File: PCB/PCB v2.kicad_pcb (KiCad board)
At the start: 4 copper layers, 56 x 45 mm, 132 parts, among them J2 USB_C_Receptacle_PowerOnly_6P, J3 6871XX182122_687110182122, J5 Conn_01x03_Pin, J7 Conn_02x06_Odd_Even, U1 TPD2E2U06DCK, U11 OPA4350EA_250, U12 OPA4350EA_250, U13 OPA4350EA_250, U2 ADS131M08xPBS, U3 74LVC1G17, U4 LM27762, U6 OPA4350EA_250, U7 LP5907MFX-3.3

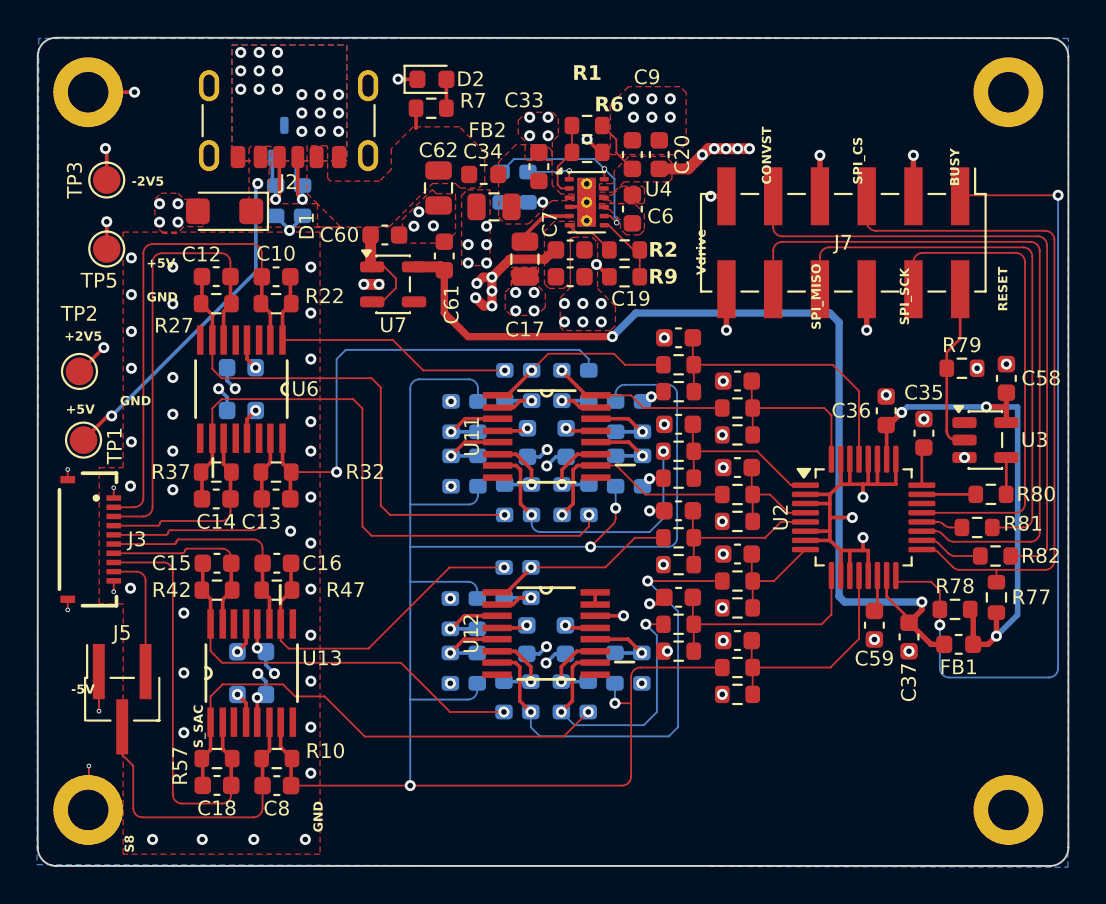
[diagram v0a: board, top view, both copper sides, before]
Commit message: Silkscreen: label the dense blocks, add channel labels and J7 pin names
Dense blocks: 0.5 mm references
- All 56 references in the dense blocks are now shown at 0.5 x 0.5 mm,
  stroke 0.12 mm.
- Divider block (front): each label sits on its part's own row. The
  left column (AIN0/2/4/6 triples) is labeled down its left side, the
  right column (AIN1/3/5/7) down its right side, so the labels read as
  two aligned lists.
  - Where a GND via sits right beside a pad, the label is allowed over
    the via's ring (vias are tented both sides) but never over the
    drill. R74 is labelled below its part.
- Diff-amp resistors and C23-C26 (back): each label is next to its own
  part and closer to it than to any neighbour.

Per-channel labels, 0.8 mm
- CH1-CH7 on B.SilkS, next to each diff-amp's four-resistor group.
  Each label is kept well clear of other channels' parts, so it can't
  be read as the wrong channel.
- AIN0-AIN7 on B.SilkS, directly behind each divider C / Rs / Rsh
  triple. There is no room for 0.8 mm text on the front between the
  two 3.2 mm-pitch columns; the back is empty there.
- Channel map (from the schematic note): AIN0=Vout1, AIN1=Vout4,
  AIN2=Vout2, AIN3=Vout3, AIN4=Vout5, AIN5=Vout6, AIN6=Vout7,
  AIN7=Vsac.

J7 pin names, 0.8 mm
- Removed the seven old 0.5 mm texts (Vdrive, CONVST, SPI_MISO,
  SPI_CS, SPI_SCK, BUSY, RESET). They were AD7606-era names and sat
  on the pads.
- New labels, outboard of each pad:
  - odd row (above): SYNC, GND, CS, GND, DRDY, GND (pins 1-11);
  - even row (below): CLK, MOSI, GND, MISO, SCLK, GND (pins 2-12).
- The odd-row labels are bottom-aligned at a common gap. CLK and the
  pin-12 GND are horizontal because R79 or a via sits right below
  those pads.
- To make room, the C35, C36, C58, R79 and U2 references were
  re-placed with the same rules as before.

Only silkscreen changes: no footprint, track, via or zone moved.
DRC: no new silk_overlap or silk_over_copper items; the text_height
warnings rise from 17 to 66, a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
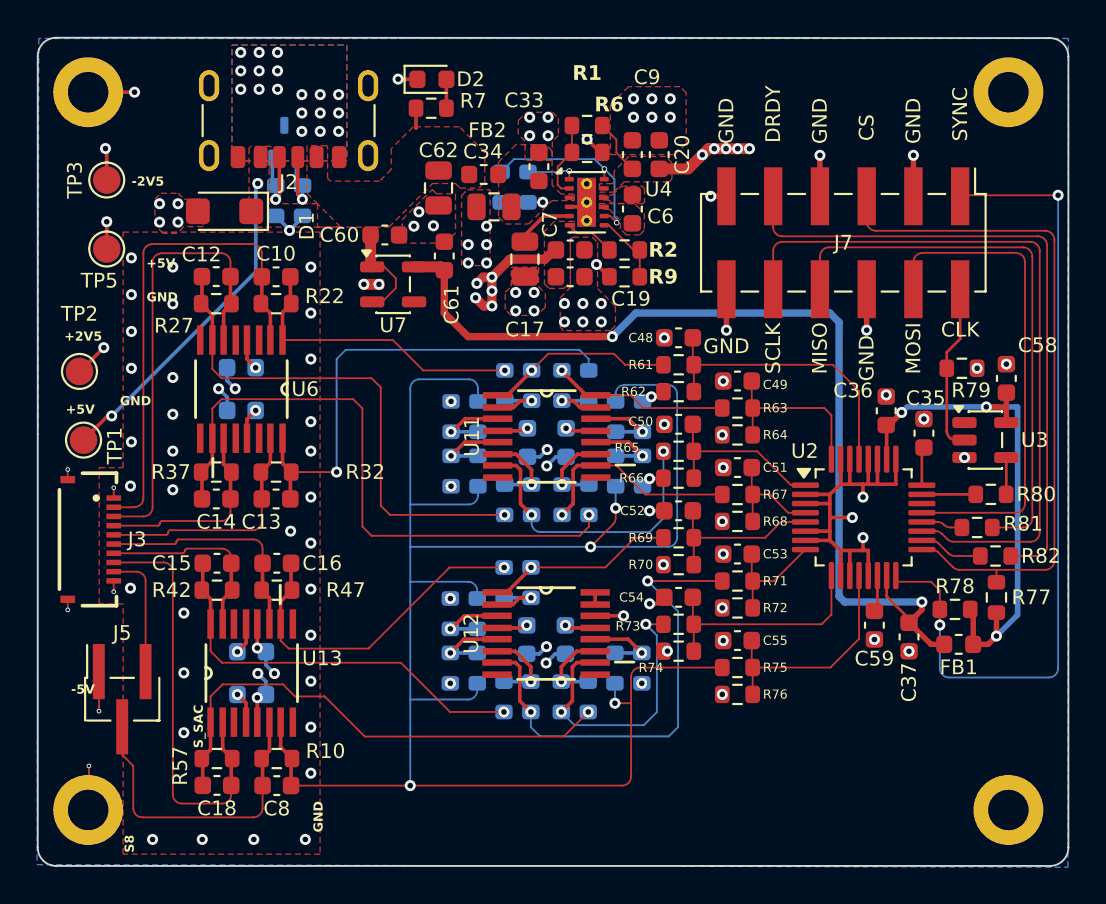
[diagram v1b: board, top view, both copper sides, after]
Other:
- board text added: "AIN0"
- board text added: "AIN1"
- board text added: "AIN2"
- board text added: "AIN3"
- board text added: "AIN4"
- board text added: "AIN5"
- board text added: "AIN6"
- board text added: "AIN7"
- board text added: "CH1"
- board text added: "CH2"
- board text added: "CH3"
- board text added: "CH4"
- board text added: "CH5"
- board text added: "CH6"
- board text added: "CH7"
- board text added: "CLK"
- board text added: "CS"
- board text added: "DRDY"
- board text added: "MISO"
- board text added: "MOSI"
- board text added: "SCLK"
- board text added: "SYNC"
- board text removed: "BUSY"
- board text removed: "CONVST"
- board text removed: "RESET"
- board text removed: "SPI_CS"
- board text removed: "SPI_MISO"
- board text removed: "SPI_SCK"
- board text removed: "Vdrive"

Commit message: Silkscreen: fix stale power and J5 labels
Several 0.5 mm user texts dated from an earlier layout and no longer
matched the parts next to them.

- TP5 (GND): the "+5V" text beside it becomes "GND", placed the way
  TP3's "-2V5" label is. The duplicate loose "GND" just below it,
  at (127.17, 90.43), is removed.
- Removed an orphan "-5V" at (123.07, 111.74). No -5V net exists on
  this board, and the text also sat on J5 pin 1 (silk_over_copper).
- Removed a loose "GND" at (125.72, 96.07), between TP2 and TP1. It
  labelled no test point.
- J5: the old "S8", "S_SAC" and "GND" texts were left at the previous
  2.54 mm J5 position. They are replaced by pin labels at the 1.27 mm
  J5: GND above pin 1, S8 above pin 3 (either side of the J5
  designator), S_SAC to the left of pin 2.

Every remaining user text now labels an adjacent pin or test point:
- +2V5 at TP2, +5V at TP1, -2V5 at TP3, GND at TP5;
- GND, S_SAC and S8 at J5.
New labels keep the existing style: 0.5 mm, bold, knockout.

DRC: silk_over_copper 1 -> 0, silk_overlap 3 -> 2, text_height
66 -> 63. No footprint, track, via or zone moved.

Co-Authored-By: Claude Opus 5.5 <noreply@anthropic.com>
Claude-Session: https://claude.ai/code/session_01TYMP7BCHvS3DvLnCv8UeQA
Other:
- board text removed: "-5V"
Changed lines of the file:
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@@
-		)
-	)
-	(gr_text "-5V"
-		(at 123.07 111.74 0)
-		(layer "F.SilkS" knockout)
-		(effects
-			(font
-				(size 0.5 0.5)
-				(thickness 0.125)
-				(bold yes)
-			)
-			(justify left bottom)
-		)
-	)
-	(gr_text "GND\n"
-		(at 125.72 96.07 0)
-		(layer "F.SilkS" knockout)
-		(effects
-			(font
-				(size 0.5 0.5)
-				(thickness 0.125)
-				(bold yes)
-			)
-			(justify left bottom)
 		)
 	)
@@
 		)
 	)
-	(gr_text "+5V"
-		(at 127.16 88.59 0)
-		(layer "F.SilkS" knockout)
-		(effects
-			(font
-				(size 0.5 0.5)
-				(thickness 0.125)
-				(bold yes)
-			)
-			(justify left bottom)
-		)
-	)
-	(gr_text "GND\n"
-		(at 127.17 90.43 0)
-		(layer "F.SilkS" knockout)
-		(effects
-			(font
-				(size 0.5 0.5)
-				(thickness 0.125)
-				(bold yes)
-			)
-			(justify left bottom)
-		)
-	)
-	(gr_text "S8"
-		(at 126.54 120.32 90)
-		(layer "F.SilkS" knockout)
-		(effects
-			(font
-				(size 0.5 0.5)
-				(thickness 0.125)
-				(bold yes)
-			)
-			(justify left bottom)
-		)
-	)
-	(gr_text "S_SAC"
-		(at 130.29 114.64 90)
+	(gr_text "GND"
+		(at 126.36 87.89 0)
 		(layer "F.SilkS" knockout)
 		(effects
@@
 	)
 	(gr_text "GND"
-		(at 136.8 119.22 90)
+		(at 123.38 108.48 0)
 		(layer "F.SilkS" knockout)
 		(effects
@@
 				(bold yes)
 			)
-			(justify left bottom)
 		)
 	)
+	(gr_text "S_SAC"
+		(at 124.1 113.73 0)
+		(layer "F.SilkS" knockout)
+		(effects
+			(font
+				(size 0.5 0.5)
+				(thickness 0.125)
+				(bold yes)
+			)
+		)
+	)
+	(gr_text "S8"
+		(at 128.12 108.48 0)
+		(layer "F.SilkS" knockout)
+		(effects
+			(font
+				(size 0.5 0.5)
+				(thickness 0.125)
+				(bold yes)
+			)
+		)
+	)

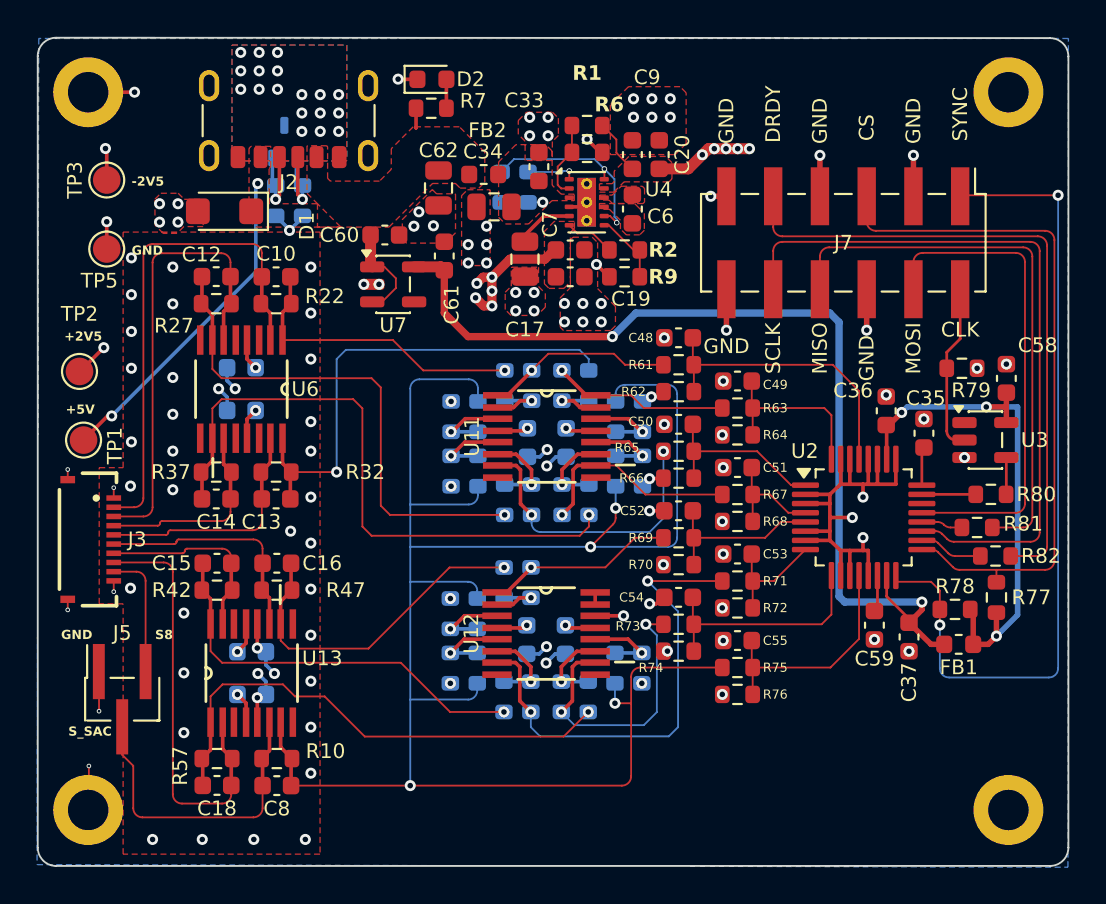
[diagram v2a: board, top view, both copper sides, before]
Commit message: Fix op-amp pin-1 marking, re-place four labels, reroute TP3's -2V5 via
Designer edits made in pcbnew after the pre-order review.

- Opa4 footprint (U6, U11, U12, U13): the silkscreen pin-1 marker now
  sits at pin 1.
  - The notch was on the body edge, so the placed IC hid it.
  - The only visible mark was a bar beside the pin 9/10 corner, which
    read as pin 1 at the wrong end. Fitting the part 180 deg round
    would put the supplies on the inputs.
  - The embedded footprint's unit table is dropped as well.
  - This also clears both DRC silk_overlap items (R37/U6, U13/R47).
- Re-placed the C9, C19, R1 and R6 reference labels. The review found
  them sitting on, or equidistant from, a neighbouring part.
- TP3 (-2V5): the via moves from (124.94, 82.06) to (127.21, 83.05),
  fed by a 0.2 mm F.Cu stub from the test point.

Co-Authored-By: Claude Opus 5.5 <noreply@anthropic.com>
Claude-Session: https://claude.ai/code/session_01TYMP7BCHvS3DvLnCv8UeQA
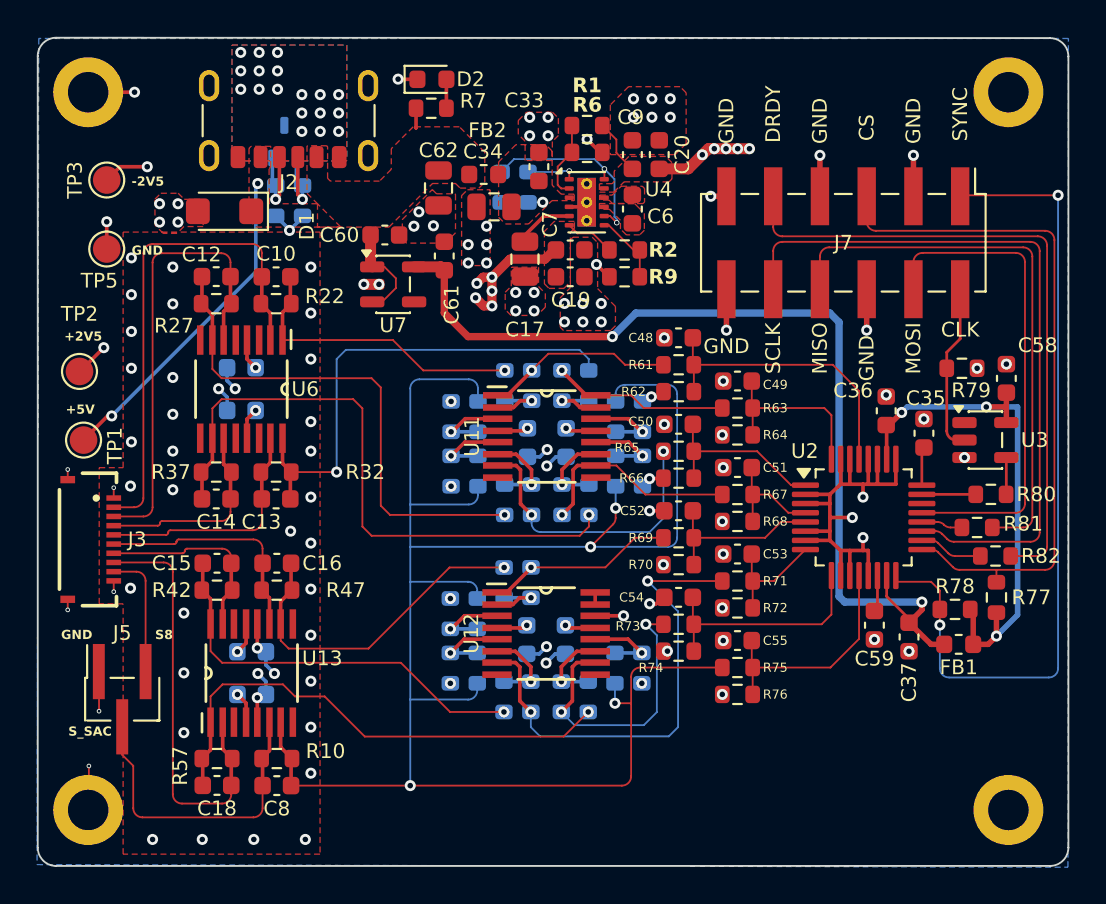
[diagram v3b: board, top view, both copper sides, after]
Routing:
- net -2V5: track 18.9 -> 19.7 mm
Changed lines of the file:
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@@
 		(tags "capacitor")
 		(property "Reference" "C19"
-			(at -3.3 -1.2 0)
+			(at -0.03 -1.25 180)
 			(layer "F.SilkS")
 			(effects
@@
 		(tags "capacitor")
 		(property "Reference" "C9"
-			(at 4.2 0.8 0)
+			(at 2.03 -0.09 0)
 			(layer "F.SilkS")
 			(effects
@@
 		(sheetname "/SENSORS/")
 		(sheetfile "FOGLIO2.kicad_sch")
-		(units
-			(unit
-				(name "A")
-				(pins "3" "2" "8" "9" "1")
-			)
-			(unit
-				(name "B")
-				(pins "5" "6" "7")
-			)
-			(unit
-				(name "C")
-				(pins "12" "11" "10")
-			)
-			(unit
-				(name "D")
-				(pins "14" "15" "16")
-			)
-			(unit
-				(name "E")
-				(pins "4" "13")
-			)
-		)
 		(attr smd)
 		(duplicate_pad_numbers_are_jumpers no)
@@
 		)
 		(fp_line
-			(start 4.7752 1.5494)
-			(end 3.7592 1.5494)
+			(start -0.3048 -2.4892)
+			(end -1.5494 -2.4892)
 			(stroke
 				(width 0.1524)
@@
 		)
 		(fp_line
-			(start -0.3048 -2.4892)
-			(end -1.5494 -2.4892)
+			(start 0.3048 -2.4892)
+			(end -0.3048 -2.4892)
 			(stroke
 				(width 0.1524)
@@
 		)
 		(fp_line
-			(start 0.3048 -2.4892)
-			(end -0.3048 -2.4892)
+			(start 1.5494 -2.4892)
+			(end 0.3048 -2.4892)
 			(stroke
 				(width 0.1524)
@@
 		)
 		(fp_line
-			(start 1.5494 -2.4892)
-			(end 0.3048 -2.4892)
+			(start -2.192 -2.7)
+			(end -3.208 -2.7)
 			(stroke
 				(width 0.1524)
@@
 		(tags "SparkFun resistor")
 		(property "Reference" "R6"
-			(at 1.2 -2.6 0)
+			(at 0.01 -2.58 0)
 			(layer "F.SilkS")
 			(effects
@@
 		(sheetname "/SENSORS/")
 		(sheetfile "FOGLIO2.kicad_sch")
-		(units
-			(unit
-				(name "A")
-				(pins "3" "2" "8" "9" "1")
-			)
-			(unit
-				(name "B")
-				(pins "5" "6" "7")
-			)
-			(unit
-				(name "C")
-				(pins "12" "11" "10")
-			)
-			(unit
-				(name "D")
-				(pins "14" "15" "16")
-			)
-			(unit
-				(name "E")
-				(pins "4" "13")
-			)
-		)
 		(attr smd)
 		(duplicate_pad_numbers_are_jumpers no)
 		(fp_line
+			(start -2.192 -2.7)
+			(end -3.208 -2.7)
+			(stroke
+				(width 0.1524)
+				(type solid)
+			)
+			(layer "F.SilkS")
+		)
+		(fp_line
 			(start -1.5494 2.4892)
 			(end 1.5494 2.4892)
@@
 			(layer "F.SilkS")
 		)
-		(fp_line
-			(start 4.7752 1.5494)
-			(end 3.7592 1.5494)
-			(stroke
-				(width 0.1524)
-				(type solid)
-			)
-			(layer "F.SilkS")
-		)
 		(fp_arc
 			(start 0.3048 -2.4892)
@@
 		(tags "SparkFun resistor")
 		(property "Reference" "R1"
-			(at 0 2.85 0)
+			(at 0 2.18 0)
 			(layer "F.SilkS")
 			(effects
@@
 		(sheetname "/SENSORS/")
 		(sheetfile "FOGLIO2.kicad_sch")
-		(units
-			(unit
-				(name "A")
-				(pins "3" "2" "8" "9" "1")
-			)
-			(unit
-				(name "B")
-				(pins "5" "6" "7")
-			)
-			(unit
-				(name "C")
-				(pins "12" "11" "10")
-			)
-			(unit
-				(name "D")
-				(pins "14" "15" "16")
-			)
-			(unit
-				(name "E")
-				(pins "4" "13")
-			)
-		)
 		(attr smd)
 		(duplicate_pad_numbers_are_jumpers no)
 		(fp_line
-			(start 1.5494 -2.4892)
-			(end 0.3048 -2.4892)
+			(start -2.192 -2.7)
+			(end -3.208 -2.7)
 			(stroke
 				(width 0.1524)
@@
 		)
 		(fp_line
-			(start 0.3048 -2.4892)
-			(end -0.3048 -2.4892)
+			(start 1.5494 -2.4892)
+			(end 0.3048 -2.4892)
 			(stroke
 				(width 0.1524)
@@
 		)
 		(fp_line
-			(start -0.3048 -2.4892)
-			(end -1.5494 -2.4892)
+			(start 0.3048 -2.4892)
+			(end -0.3048 -2.4892)
 			(stroke
 				(width 0.1524)
@@
 		)
 		(fp_line
-			(start 4.7752 1.5494)
-			(end 3.7592 1.5494)
+			(start -0.3048 -2.4892)
+			(end -1.5494 -2.4892)
 			(stroke
 				(width 0.1524)
@@
 		(sheetname "/SENSORS/")
 		(sheetfile "FOGLIO2.kicad_sch")
-		(units
-			(unit
-				(name "A")
-				(pins "3" "2" "8" "9" "1")
-			)
-			(unit
-				(name "B")
-				(pins "5" "6" "7")
-			)
-			(unit
-				(name "C")
-				(pins "12" "11" "10")
-			)
-			(unit
-				(name "D")
-				(pins "14" "15" "16")
-			)
-			(unit
-				(name "E")
-				(pins "4" "13")
-			)
-		)
 		(attr smd)
 		(duplicate_pad_numbers_are_jumpers no)
 		(fp_line
+			(start -2.184 -2.7)
+			(end -3.2 -2.7)
+			(stroke
+				(width 0.1524)
+				(type solid)
+			)
+			(layer "F.SilkS")
+		)
+		(fp_line
 			(start -1.5494 2.4892)
 			(end 1.5494 2.4892)
@@
 			(layer "F.SilkS")
 		)
-		(fp_line
-			(start 4.7752 1.5494)
-			(end 3.7592 1.5494)
-			(stroke
-				(width 0.1524)
-				(type solid)
-			)
-			(layer "F.SilkS")
-		)
 		(fp_arc
 			(start 0.3048 -2.4892)
@@
 	)
 	(segment
-		(start 125.009426 83.771476)
-		(end 125.009426 82.129426)
-		(width 0.2)
-		(layer "F.Cu")
-		(net "-2V5")
-	)
-	(segment
-		(start 125.009426 82.129426)
-		(end 124.94 82.06)
-		(width 0.2)
-		(layer "F.Cu")
-		(net "-2V5")
-	)
-	(segment
 		(start 132.5804 107.895)
 		(end 132.5804 108.9314)
@@
 	)
 	(segment
+		(start 127.21 83.05)
+		(end 125.730902 83.05)
+		(width 0.2)
+		(layer "F.Cu")
+		(net "-2V5")
+	)
+	(segment
 		(start 150.071529 108.109044)
 		(end 149.931329 107.968844)
@@
 	)
 	(segment
+		(start 125.730902 83.05)
+		(end 125.009426 83.771476)
+		(width 0.2)
+		(layer "F.Cu")
+		(net "-2V5")
+	)
+	(segment
 		(start 146.92 88.07)
 		(end 145.94 89.05)
@@
 	)
 	(via
-		(at 124.94 82.06)
+		(at 127.21 83.05)
 		(size 0.6)
 		(drill 0.3)
